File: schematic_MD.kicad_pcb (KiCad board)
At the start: 2 copper layers, 100 x 100 mm, 19 parts, among them J7 Conn_02x01, J8 Conn_02x01, J9 Conn_02x01, Q1 NMOS, Q2 NMOS, Q3 NMOS, Q4 NMOS, Q5 NMOS, Q6 NMOS, Q7 NMOS, Q8 NMOS, U2 NJM12877F, U6 STM32F405RGTx, U7 MAX3051, U8 L78M05ABDT-TR

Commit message: add footprint
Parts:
- added C1: 330u, Capacitor_THT:CP_Radial_D10.0mm_P5.00mm, F.Cu at (99.5, 59.9)
- added C10: 330u, Capacitor_THT:CP_Radial_D10.0mm_P5.00mm, F.Cu at (111.0, 60.0)
- added C11: 330u, Capacitor_THT:CP_Radial_D10.0mm_P5.00mm, F.Cu at (174.0, 61.4)
- added C12: 330u, Capacitor_THT:CP_Radial_D10.0mm_P5.00mm, F.Cu at (186.3, 61.4)
- added C2: 100u, Capacitor_THT:CP_Radial_D6.3mm_P2.50mm, F.Cu at (140.4, 126.9)
- added C8: 100u, Capacitor_THT:CP_Radial_D6.3mm_P2.50mm, F.Cu at (143.0, 103.0)
- added C9: 100u, Capacitor_THT:CP_Radial_D6.3mm_P2.50mm, F.Cu at (138.5, 93.9)
- added J10: Gate_PWR_Jump, Connector_PinHeader_2.54mm:PinHeader_1x02_P2.54mm_Vertical, F.Cu at (167.3, 71.2)
- added J11: Gate_PWR_Jump, Connector_PinHeader_2.54mm:PinHeader_1x02_P2.54mm_Vertical, F.Cu at (122.1, 71.3)
- added J12: EXPWR_GND, Connector_PinHeader_2.54mm:PinHeader_1x02_P2.54mm_Vertical, F.Cu at (161.3, 68.7)
- added J13: EXPWR_GND, Connector_PinHeader_2.54mm:PinHeader_1x02_P2.54mm_Vertical, F.Cu at (128.3, 68.9)
- added J4: CAN_Bus, Connector_JST:JST_XA_B04B-XASK-1_1x04_P2.50mm_Vertical, F.Cu at (141.2, 135.7)
- added J5: Rotaly_encoder_1, Connector_JST:JST_XA_B05B-XASK-1_1x05_P2.50mm_Vertical, F.Cu at (125.0, 135.7)
- added J6: Rotaly_encoder_2, Connector_JST:JST_XA_B05B-XASK-1_1x05_P2.50mm_Vertical, F.Cu at (154.8, 135.7)
- added R1: 10k, Resistor_SMD:R_1206_3216Metric_Pad1.30x1.75mm_HandSolder, F.Cu at (141.9, 118.4)
- added R14: 10k, Resistor_SMD:R_1206_3216Metric_Pad1.30x1.75mm_HandSolder, F.Cu at (144.8, 67.3)
- added R15: 120, Resistor_SMD:R_0603_1608Metric_Pad0.98x0.95mm_HandSolder, F.Cu at (148.7, 126.4)
- added SW1: SW_MEC_5G, Button_Switch_THT:SW_PUSH_6mm, F.Cu at (120.8, 122.5)
- J7, J8: value Conn_02x01 -> Z_jumper
- moved Q1 81.7 mm to (117.3, 111.7), turned to 90 degrees
- moved J8 71.6 mm to (162.2, 123.8)
- moved Q2 64.6 mm to (117.3, 100.1), turned to 90 degrees
- moved J7 59.3 mm to (132.6, 124.7)
- moved U1 55.5 mm to (125.4, 102.9), turned to 180 degrees
- moved Q3 52.3 mm to (117.3, 88.6), turned to 90 degrees
- moved J9 49.1 mm to (150.0, 129.0), turned to -90 degrees
- moved Q4 48.6 mm to (117.3, 77.0), turned to 90 degrees
- moved U7 37.7 mm to (148.0, 122.8), turned to -90 degrees
- moved U8 37.6 mm to (138.0, 112.4), turned to 180 degrees
- moved U6 27.7 mm to (145.0, 78.2)
- moved U3 27.6 mm to (125.2, 80.3), turned to 180 degrees
- moved Q5 23.9 mm to (173.3, 73.2)
- moved Q7 23.9 mm to (173.3, 96.3)
- moved Q8 23.9 mm to (173.3, 107.9)
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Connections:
- U1 pad 11: Vdrive -> /Driver/H-bridge_left
- U3 pad 11: Vdrive -> /Driver/H-bridge_right
- U4 pad 11: Vdrive -> /Driver1/H-bridge_left
- U5 pad 11: Vdrive -> /Driver1/H-bridge_right

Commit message: pattern update
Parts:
- added J1: XT60, RDC_footprint:XT60, F.Cu at (146.3, 49.8)
- added J2: XT60, RDC_footprint:XT60, F.Cu at (184.4, 136.1)
- added J3: XT60, RDC_footprint:XT60, F.Cu at (105.6, 136.1)
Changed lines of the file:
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@@
     )
+  )
+  (footprint "RDC_footprint:XT60" (layer "F.Cu")
+    (at 146.26 49.77)
+    (descr "XT60 connector constant 30A peak current of 60A")
+    (tags "XT60")
+    (property "Sheetfile" "schematic_MD.kicad_sch")
+    (property "Sheetname" "")
+    (property "ki_description" "Generic connector, single row, 01x02, script generated (kicad-library-utils/schlib/autogen/connector/)")
+    (property "ki_keywords" "connector")
+    (attr through_hole)
+    (fp_text reference "J1" (at 0 1.3 unlocked) (layer "F.SilkS")
+        (effects (font (size 1 1) (thickness 0.1)))
+    )
+    (fp_text value "XT60" (at 0 2.8 unlocked) (layer "F.Fab")
+        (effects (font (size 1 1) (thickness 0.15)))
+    )
+    (fp_text user "+" (at -10.25 -3.35 unlocked) (layer "F.SilkS")
+        (effects (font (size 2 2) (thickness 0.2)) (justify left bottom))
+    )
+    (fp_text user "${REFERENCE}" (at 0 4.3 unlocked) (layer "F.Fab")
+        (effects (font (size 1 1) (thickness 0.15)))
+    )
+    (fp_line (start -7.75 -8.3) (end 5.25 -8.3)
+      (stroke (width 0.1) (type default)) (layer "F.SilkS"))
+    (fp_line (start -7.75 0.2) (end -7.75 -8.3)
+      (stroke (width 0.1) (type default)) (layer "F.SilkS"))
+    (fp_line (start -7.75 0.2) (end 5.25 0.2)
+      (stroke (width 0.1) (type default)) (layer "F.SilkS"))
+    (fp_line (start 5.25 -8.3) (end 7.75 -5.8)
+      (stroke (width 0.1) (type default)) (layer "F.SilkS"))
+    (fp_line (start 5.25 0.2) (end 7.75 -2.3)
+      (stroke (width 0.1) (type default)) (layer "F.SilkS"))
+    (fp_line (start 7.75 -5.8) (end 7.75 -2.3)
+      (stroke (width 0.1) (type default)) (layer "F.SilkS"))
+    (pad "1" thru_hole circle (at -3.6 -4.05) (size 6 6) (drill 3.7) (layers "*.Cu" "*.Mask")
+      (net 3 "/Driver/H-bridge_left") (pinfunction "Pin_1") (pintype "passive"))
+    (pad "2" thru_hole circle (at 3.6 -4.05) (size 6 6) (drill 3.7) (layers "*.Cu" "*.Mask")
+      (net 7 "/Driver/H-bridge_right") (pinfunction "Pin_2") (pintype "passive"))
   )
   (footprint "Connector_JST:JST_XA_B05B-XASK-1_1x05_P2.50mm_Vertical" (layer "F.Cu")
@@
     )
   )
+  (footprint "RDC_footprint:XT60" (layer "F.Cu")
+    (at 184.36 136.13)
+    (descr "XT60 connector constant 30A peak current of 60A")
+    (tags "XT60")
+    (property "Sheetfile" "schematic_MD.kicad_sch")
+    (property "Sheetname" "")
+    (property "ki_description" "Generic connector, single row, 01x02, script generated (kicad-library-utils/schlib/autogen/connector/)")
+    (property "ki_keywords" "connector")
+    (attr through_hole)
+    (fp_text reference "J2" (at 0 1.3 unlocked) (layer "F.SilkS")
+        (effects (font (size 1 1) (thickness 0.1)))
+    )
+    (fp_text value "XT60" (at 0 2.8 unlocked) (layer "F.Fab")
+        (effects (font (size 1 1) (thickness 0.15)))
+    )
+    (fp_text user "+" (at -10.25 -3.35 unlocked) (layer "F.SilkS")
+        (effects (font (size 2 2) (thickness 0.2)) (justify left bottom))
+    )
+    (fp_text user "${REFERENCE}" (at 0 4.3 unlocked) (layer "F.Fab")
+        (effects (font (size 1 1) (thickness 0.15)))
+    )
+    (fp_line (start -7.75 -8.3) (end 5.25 -8.3)
+      (stroke (width 0.1) (type default)) (layer "F.SilkS"))
+    (fp_line (start -7.75 0.2) (end -7.75 -8.3)
+      (stroke (width 0.1) (type default)) (layer "F.SilkS"))
+    (fp_line (start -7.75 0.2) (end 5.25 0.2)
+      (stroke (width 0.1) (type default)) (layer "F.SilkS"))
+    (fp_line (start 5.25 -8.3) (end 7.75 -5.8)
+      (stroke (width 0.1) (type default)) (layer "F.SilkS"))
+    (fp_line (start 5.25 0.2) (end 7.75 -2.3)
+      (stroke (width 0.1) (type default)) (layer "F.SilkS"))
+    (fp_line (start 7.75 -5.8) (end 7.75 -2.3)
+      (stroke (width 0.1) (type default)) (layer "F.SilkS"))
+    (pad "1" thru_hole circle (at -3.6 -4.05) (size 6 6) (drill 3.7) (layers "*.Cu" "*.Mask")
+      (net 10 "/Driver1/H-bridge_left") (pinfunction "Pin_1") (pintype "passive"))
+    (pad "2" thru_hole circle (at 3.6 -4.05) (size 6 6) (drill 3.7) (layers "*.Cu" "*.Mask")
+      (net 13 "/Driver1/H-bridge_right") (pinfunction "Pin_2") (pintype "passive"))
+  )
   (footprint "Connector_PinHeader_2.54mm:PinHeader_1x02_P2.54mm_Vertical" (layer "F.Cu")
     (at 122.1 71.3 180)
@@
     )
   )
+  (footprint "RDC_footprint:XT60" (layer "F.Cu")
+    (at 105.62 136.13)
+    (descr "XT60 connector constant 30A peak current of 60A")
+    (tags "XT60")
+    (property "Sheetfile" "schematic_MD.kicad_sch")
+    (property "Sheetname" "")
+    (property "ki_description" "Generic connector, single row, 01x02, script generated (kicad-library-utils/schlib/autogen/connector/)")
+    (property "ki_keywords" "connector")
+    (attr through_hole)
+    (fp_text reference "J3" (at 0 1.3 unlocked) (layer "F.SilkS")
+        (effects (font (size 1 1) (thickness 0.1)))
+    )
+    (fp_text value "XT60" (at 0 2.8 unlocked) (layer "F.Fab")
+        (effects (font (size 1 1) (thickness 0.15)))
+    )
+    (fp_text user "+" (at -10.25 -3.35 unlocked) (layer "F.SilkS")
+        (effects (font (size 2 2) (thickness 0.2)) (justify left bottom))
+    )
+    (fp_text user "${REFERENCE}" (at 0 4.3 unlocked) (layer "F.Fab")
+        (effects (font (size 1 1) (thickness 0.15)))
+    )
+    (fp_line (start -7.75 -8.3) (end 5.25 -8.3)
+      (stroke (width 0.1) (type default)) (layer "F.SilkS"))
+    (fp_line (start -7.75 0.2) (end -7.75 -8.3)
+      (stroke (width 0.1) (type default)) (layer "F.SilkS"))
+    (fp_line (start -7.75 0.2) (end 5.25 0.2)
+      (stroke (width 0.1) (type default)) (layer "F.SilkS"))
+    (fp_line (start 5.25 -8.3) (end 7.75 -5.8)
+      (stroke (width 0.1) (type default)) (layer "F.SilkS"))
+    (fp_line (start 5.25 0.2) (end 7.75 -2.3)
+      (stroke (width 0.1) (type default)) (layer "F.SilkS"))
+    (fp_line (start 7.75 -5.8) (end 7.75 -2.3)
+      (stroke (width 0.1) (type default)) (layer "F.SilkS"))
+    (pad "1" thru_hole circle (at -3.6 -4.05) (size 6 6) (drill 3.7) (layers "*.Cu" "*.Mask")
+      (net 1 "Vdrive") (pinfunction "Pin_1") (pintype "passive"))
+    (pad "2" thru_hole circle (at 3.6 -4.05) (size 6 6) (drill 3.7) (layers "*.Cu" "*.Mask")
+      (net 5 "GND2") (pinfunction "Pin_2") (pintype "passive"))
+  )
   (footprint "Connector_JST:JST_XA_B04B-XASK-1_1x04_P2.50mm_Vertical" (layer "F.Cu")

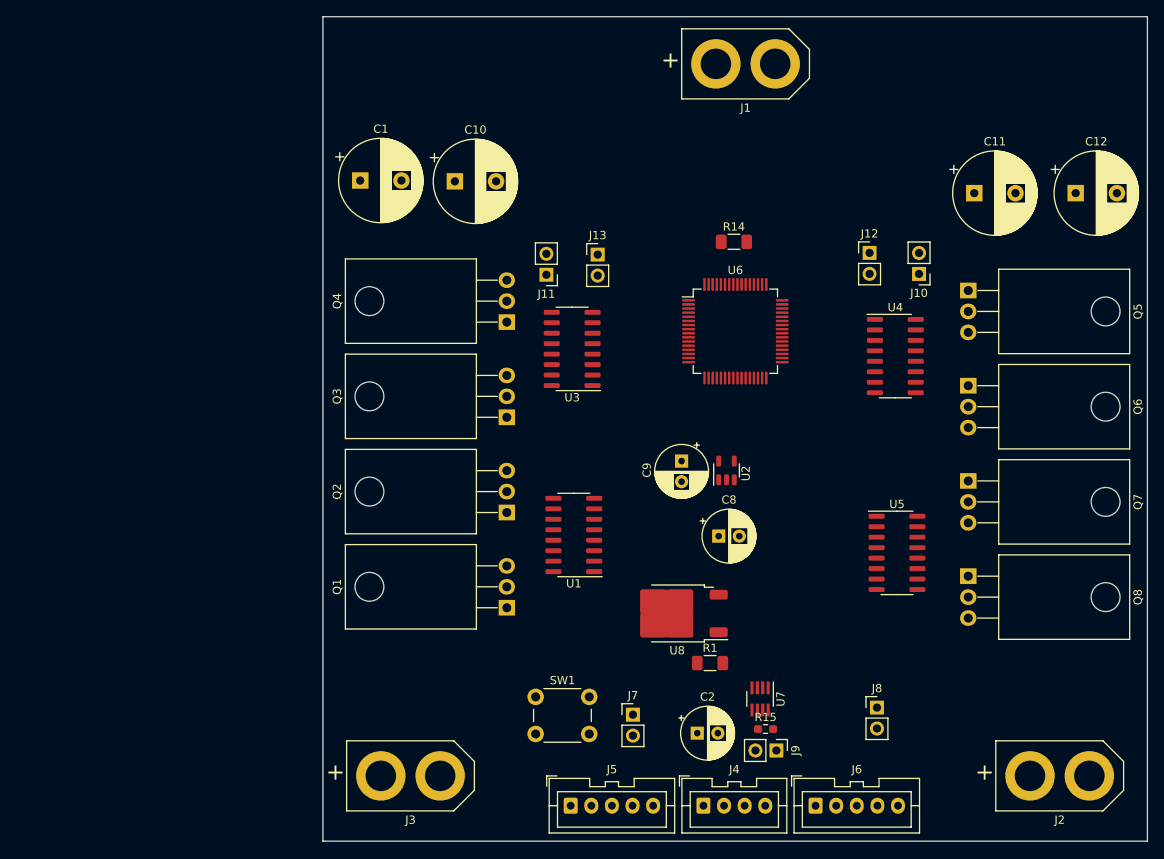
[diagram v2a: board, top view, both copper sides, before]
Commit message: Update motor driver circuit
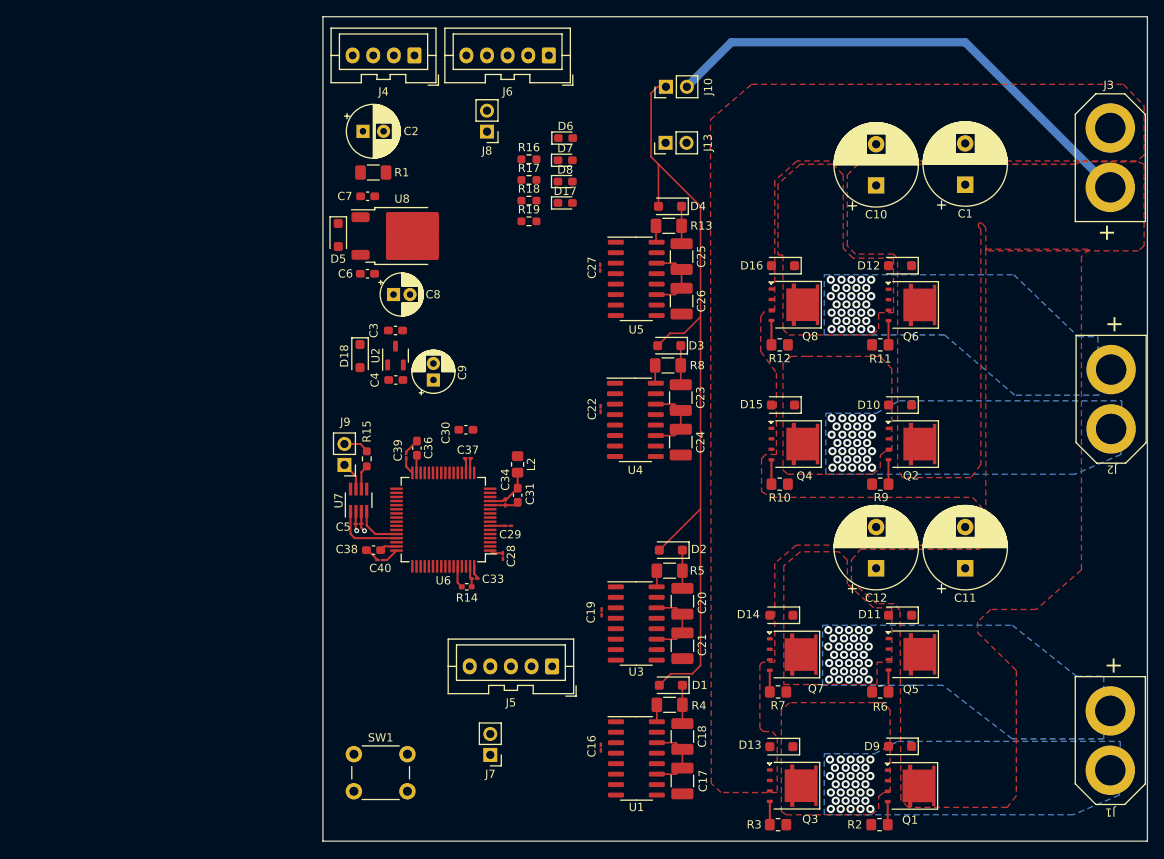
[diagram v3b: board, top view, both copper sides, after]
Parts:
- removed J11: Gate_PWR_Jump, Connector_PinHeader_2.54mm:PinHeader_1x02_P2.54mm_Vertical
- removed J12: EXPWR_GND, Connector_PinHeader_2.54mm:PinHeader_1x02_P2.54mm_Vertical
- added C16: 0.1u, Capacitor_SMD:C_01005_0402Metric_Pad0.57x0.30mm_HandSolder, F.Cu at (128.7, 128.7)
- added C17: 10u, Capacitor_SMD:C_1210_3225Metric_Pad1.33x2.70mm_HandSolder, F.Cu at (138.6, 132.7)
- added C18: 10u, Capacitor_SMD:C_1210_3225Metric_Pad1.33x2.70mm_HandSolder, F.Cu at (138.6, 127.3)
- added C19: 0.1u, Capacitor_SMD:C_01005_0402Metric_Pad0.57x0.30mm_HandSolder, F.Cu at (128.8, 112.2)
- added C20: 10u, Capacitor_SMD:C_1210_3225Metric_Pad1.33x2.70mm_HandSolder, F.Cu at (138.6, 110.9)
- added C21: 10u, Capacitor_SMD:C_1210_3225Metric_Pad1.33x2.70mm_HandSolder, F.Cu at (138.6, 116.3)
- added C22: 0.1u, Capacitor_SMD:C_01005_0402Metric_Pad0.57x0.30mm_HandSolder, F.Cu at (128.7, 87.6)
- added C23: 10u, Capacitor_SMD:C_1210_3225Metric_Pad1.33x2.70mm_HandSolder, F.Cu at (138.4, 86.2)
- added C24: 10u, Capacitor_SMD:C_1210_3225Metric_Pad1.33x2.70mm_HandSolder, F.Cu at (138.4, 91.6)
- added C25: 10u, Capacitor_SMD:C_1210_3225Metric_Pad1.33x2.70mm_HandSolder, F.Cu at (138.5, 69.1)
- added C26: 10u, Capacitor_SMD:C_1210_3225Metric_Pad1.33x2.70mm_HandSolder, F.Cu at (138.5, 74.5)
- added C27: 0.1u, Capacitor_SMD:C_01005_0402Metric_Pad0.57x0.30mm_HandSolder, F.Cu at (128.6, 70.4)
- added C28: 0.1u, Capacitor_SMD:C_01005_0402Metric_Pad0.57x0.30mm_HandSolder, F.Cu at (116.8, 105.4)
- added C29: 0.1u, Capacitor_SMD:C_01005_0402Metric_Pad0.57x0.30mm_HandSolder, F.Cu at (117.5, 101.8)
- added C3: 1uF, Capacitor_SMD:C_0603_1608Metric_Pad1.08x0.95mm_HandSolder, F.Cu at (103.8, 78.1)
- added C30: 4.7uF, Capacitor_SMD:C_0603_1608Metric_Pad1.08x0.95mm_HandSolder, F.Cu at (112.3, 90.1)
- added C31: 1uF, Capacitor_SMD:C_0603_1608Metric_Pad1.08x0.95mm_HandSolder, F.Cu at (118.6, 98.0)
- added C33: 0.1u, Capacitor_SMD:C_01005_0402Metric_Pad0.57x0.30mm_HandSolder, F.Cu at (113.4, 108.2)
- added C34: 0.1u, Capacitor_SMD:C_01005_0402Metric_Pad0.57x0.30mm_HandSolder, F.Cu at (117.1, 98.9)
- added C36: 2.2uF, Capacitor_SMD:C_0603_1608Metric_Pad1.08x0.95mm_HandSolder, F.Cu at (106.4, 92.3)
- added C37: 0.1u, Capacitor_SMD:C_01005_0402Metric_Pad0.57x0.30mm_HandSolder, F.Cu at (112.6, 93.5)
- added C38: 2.2uF, Capacitor_SMD:C_0603_1608Metric_Pad1.08x0.95mm_HandSolder, F.Cu at (101.1, 104.7)
- added C39: 0.1u, Capacitor_SMD:C_01005_0402Metric_Pad0.57x0.30mm_HandSolder, F.Cu at (105.1, 93.2)
- added C4: 1uF, Capacitor_SMD:C_0603_1608Metric_Pad1.08x0.95mm_HandSolder, F.Cu at (103.8, 84.1)
- added C40: 0.1u, Capacitor_SMD:C_01005_0402Metric_Pad0.57x0.30mm_HandSolder, F.Cu at (102.0, 105.9)
- added C5: 0.1u, Capacitor_SMD:C_01005_0402Metric_Pad0.57x0.30mm_HandSolder, F.Cu at (99.3, 101.5)
- added C6: 0.1u, Capacitor_SMD:C_0603_1608Metric_Pad1.08x0.95mm_HandSolder, F.Cu at (100.4, 71.2)
- added C7: 0.1u, Capacitor_SMD:C_0603_1608Metric_Pad1.08x0.95mm_HandSolder, F.Cu at (100.4, 61.8)
- added D1: D_Schottky, Diode_SMD:D_SOD-123F, F.Cu at (137.2, 121.1)
- added D10: D_Schottky, Diode_SMD:D_SOD-123F, F.Cu at (165.0, 87.1)
- added D11: D_Schottky, Diode_SMD:D_SOD-123F, F.Cu at (165.0, 112.6)
- added D12: D_Schottky, Diode_SMD:D_SOD-123F, F.Cu at (165.0, 70.2)
- added D13: D_Schottky, Diode_SMD:D_SOD-123F, F.Cu at (150.6, 128.5)
- added D14: D_Schottky, Diode_SMD:D_SOD-123F, F.Cu at (150.6, 112.6)
- added D15: D_Schottky, Diode_SMD:D_SOD-123F, F.Cu at (150.8, 87.1)
- added D16: D_Schottky, Diode_SMD:D_SOD-123F, F.Cu at (150.8, 70.2)
- added D17: LED, LED_SMD:LED_0603_1608Metric_Pad1.05x0.95mm_HandSolder, F.Cu at (124.4, 62.6)
- added D18: D_Schottky, Diode_SMD:D_SOD-123F, F.Cu at (99.5, 81.2)
- added D2: D_Schottky, Diode_SMD:D_SOD-123F, F.Cu at (137.2, 104.7)
- added D3: D_Schottky, Diode_SMD:D_SOD-123F, F.Cu at (137.0, 79.9)
- added D4: D_Schottky, Diode_SMD:D_SOD-123F, F.Cu at (137.1, 63.0)
- added D5: D_Schottky, Diode_SMD:D_SOD-123F, F.Cu at (96.9, 66.5)
- added D6: LED, LED_SMD:LED_0603_1608Metric_Pad1.05x0.95mm_HandSolder, F.Cu at (124.4, 54.7)
- added D7: LED, LED_SMD:LED_0603_1608Metric_Pad1.05x0.95mm_HandSolder, F.Cu at (124.4, 57.4)
- added D8: LED, LED_SMD:LED_0603_1608Metric_Pad1.05x0.95mm_HandSolder, F.Cu at (124.4, 60.0)
- added D9: D_Schottky, Diode_SMD:D_SOD-123F, F.Cu at (165.0, 128.5)
- added L2: 600@100MHz, Resistor_SMD:R_0805_2012Metric_Pad1.20x1.40mm_HandSolder, F.Cu at (118.6, 94.3)
- added R10: 10, Resistor_SMD:R_0805_2012Metric_Pad1.20x1.40mm_HandSolder, F.Cu at (150.4, 96.7)
- added R11: 10, Resistor_SMD:R_0805_2012Metric_Pad1.20x1.40mm_HandSolder, F.Cu at (162.6, 79.8)
- added R12: 10, Resistor_SMD:R_0805_2012Metric_Pad1.20x1.40mm_HandSolder, F.Cu at (150.4, 79.8)
- added R13: 0.1, Resistor_SMD:R_1206_3216Metric_Pad1.30x1.75mm_HandSolder, F.Cu at (136.9, 65.4)
- added R16: 330, Resistor_SMD:R_0603_1608Metric_Pad0.98x0.95mm_HandSolder, F.Cu at (120.0, 57.3)
- added R17: 680, Resistor_SMD:R_0603_1608Metric_Pad0.98x0.95mm_HandSolder, F.Cu at (120.0, 59.8)
- added R18: 2k, Resistor_SMD:R_0603_1608Metric_Pad0.98x0.95mm_HandSolder, F.Cu at (120.0, 62.3)
- added R19: 3.6k, Resistor_SMD:R_0603_1608Metric_Pad0.98x0.95mm_HandSolder, F.Cu at (120.0, 64.8)
- added R2: 10, Resistor_SMD:R_0805_2012Metric_Pad1.20x1.40mm_HandSolder, F.Cu at (162.5, 138.0)
- added R3: 10, Resistor_SMD:R_0805_2012Metric_Pad1.20x1.40mm_HandSolder, F.Cu at (150.2, 138.0)
- added R4: 0.1, Resistor_SMD:R_1206_3216Metric_Pad1.30x1.75mm_HandSolder, F.Cu at (137.1, 123.5)
- added R5: 0.1, Resistor_SMD:R_1206_3216Metric_Pad1.30x1.75mm_HandSolder, F.Cu at (137.1, 107.2)
- added R6: 10, Resistor_SMD:R_0805_2012Metric_Pad1.20x1.40mm_HandSolder, F.Cu at (162.6, 121.9)
- added R7: 10, Resistor_SMD:R_0805_2012Metric_Pad1.20x1.40mm_HandSolder, F.Cu at (150.2, 121.9)
- added R8: 0.1, Resistor_SMD:R_1206_3216Metric_Pad1.30x1.75mm_HandSolder, F.Cu at (136.8, 82.3)
- added R9: 10, Resistor_SMD:R_0805_2012Metric_Pad1.20x1.40mm_HandSolder, F.Cu at (162.6, 96.7)
- C8, C9: value 100u -> 47u; footprint Capacitor_THT:CP_Radial_D6.3mm_P2.50mm -> Capacitor_THT:CP_Radial_D5.0mm_P2.00mm
- Q1, Q2, Q3, Q4, Q5, Q6, Q7, Q8: value NMOS -> SQJ886EP-T1_GE3; footprint Package_TO_SOT_THT:TO-220-3_Horizontal_TabDown -> Package_SO:PowerPAK_SO-8L_Single
- R14: footprint Resistor_SMD:R_1206_3216Metric_Pad1.30x1.75mm_HandSolder -> Resistor_SMD:R_0402_1005Metric_Pad0.72x0.64mm_HandSolder
- U2: value NJM12877F -> XC6206P332MR-G; footprint Package_TO_SOT_SMD:SOT-23-5 -> Package_TO_SOT_SMD:SOT-23-3
- moved J3 119.0 mm to (194.6, 57.1), turned to 90 degrees
- moved J4 97.5 mm to (106.1, 44.7), turned to 180 degrees
- moved J6 96.6 mm to (122.4, 44.7), turned to 180 degrees
- moved J1 87.8 mm to (186.4, 127.8), turned to -90 degrees
- moved J8 84.4 mm to (114.9, 53.9), turned to 180 degrees
- moved C2 83.5 mm to (99.9, 53.9)
- moved C1 73.4 mm to (172.9, 60.4), turned to 90 degrees
- moved R1 72.2 mm to (101.1, 58.9)
- moved J9 62.8 mm to (97.6, 94.4), turned to 180 degrees
- moved R15 58.4 mm to (100.3, 93.6), turned to -90 degrees
- moved U8 56.6 mm to (104.6, 66.6), turned to 0 degrees
- moved Q3 56.5 mm to (151.9, 133.3), turned to 0 degrees
- moved U7 54.3 mm to (99.3, 98.7), turned to 90 degrees
- moved Q1 53.5 mm to (166.2, 133.3), turned to 0 degrees
- moved R14 52.9 mm to (112.4, 109.2)
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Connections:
- J1 pad 1: /Driver/H-bridge_left -> /Driver/H-bridge_right
- J1 pad 2: /Driver/H-bridge_right -> /Driver/H-bridge_left
- J10 pad 1: /Driver/Gate_power -> Gate_power
- J2 pad 1: /Driver1/H-bridge_left -> /Driver1/H-bridge_right
- J2 pad 2: /Driver1/H-bridge_right -> /Driver1/H-bridge_left
- Q1 pad 1: Vdrive -> /Driver/H-bridge_left
- Q1 pad 2: Net-(Q1-G) -> /Driver/H-bridge_left
- Q2 pad 1: /Driver/H-bridge_left -> /Driver1/H-bridge_left
- Q2 pad 2: Net-(Q2-G) -> /Driver1/H-bridge_left
- Q2 pad 3: GND2 -> /Driver1/H-bridge_left
- Q3 pad 1: Vdrive -> GND2
- Q3 pad 2: Net-(Q3-G) -> GND2
- Q3 pad 3: /Driver/H-bridge_right -> GND2
- Q4 pad 1: /Driver/H-bridge_right -> GND2
- Q4 pad 2: Net-(Q4-G) -> GND2
- Q5 pad 1: Vdrive -> /Driver/H-bridge_right
- Q5 pad 2: Net-(Q5-G) -> /Driver/H-bridge_right
- Q5 pad 3: /Driver1/H-bridge_left -> /Driver/H-bridge_right
- Q6 pad 1: /Driver1/H-bridge_left -> /Driver1/H-bridge_right
- Q6 pad 2: Net-(Q6-G) -> /Driver1/H-bridge_right
- Q6 pad 3: GND2 -> /Driver1/H-bridge_right
- Q7 pad 1: Vdrive -> GND2
- Q7 pad 2: Net-(Q7-G) -> GND2
- Q7 pad 3: /Driver1/H-bridge_right -> GND2
- Q8 pad 1: /Driver1/H-bridge_right -> GND2
- Q8 pad 2: Net-(Q8-G) -> GND2
- U2 pad 1: +5V -> GND1
- U2 pad 2: GND1 -> +3.3V
- U6 pad 55: unconnected-(U6-PB3-Pad55) -> /STM32F405/SWO
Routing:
- net Gate_power: track 0.00 -> 98.9 mm
- net Vdrive: track 0.00 -> 60.9 mm
- net GND1: track 0.00 -> 13.3 mm, vias 0 -> 1
- net +3.3V: track 0.00 -> 11.1 mm, vias 0 -> 1
- net /Driver/H-bridge_right: track 0.00 -> 10.9 mm, vias 0 -> 32
- net /Driver/H-bridge_left: track 0.00 -> 10.8 mm, vias 0 -> 32
- net /Driver1/H-bridge_right: track 0.00 -> 8.97 mm, vias 0 -> 32
- net /Driver1/H-bridge_left: track 0.00 -> 8.96 mm, vias 0 -> 32
- net /STM32F405/CAN_TX: track 0.00 -> 7.76 mm
- net VDDA: track 0.00 -> 5.88 mm
- net /STM32F405/CAN_RX: track 0.00 -> 4.98 mm
- net Net-(D3-K): track 0.00 -> 4.74 mm
- net Net-(D1-K): track 0.00 -> 4.65 mm
- net Net-(D2-K): track 0.00 -> 4.64 mm
- net Net-(D4-K): track 0.00 -> 4.54 mm
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- added copper zone on B.Cu, net /Driver/H-bridge_left
- added copper zone on F.Cu, net /Driver/H-bridge_left
- added copper zone on B.Cu, net /Driver/H-bridge_right
- added copper zone on F.Cu, net /Driver/H-bridge_right
- added copper zone on B.Cu, net /Driver1/H-bridge_left
- added copper zone on F.Cu, net /Driver1/H-bridge_left
- added copper zone on B.Cu, net /Driver1/H-bridge_right
- added copper zone on F.Cu, net /Driver1/H-bridge_right
- added copper zone on F.Cu, net GND2
- added copper zone on F.Cu, net Vdrive
